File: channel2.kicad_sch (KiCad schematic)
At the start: 33 parts

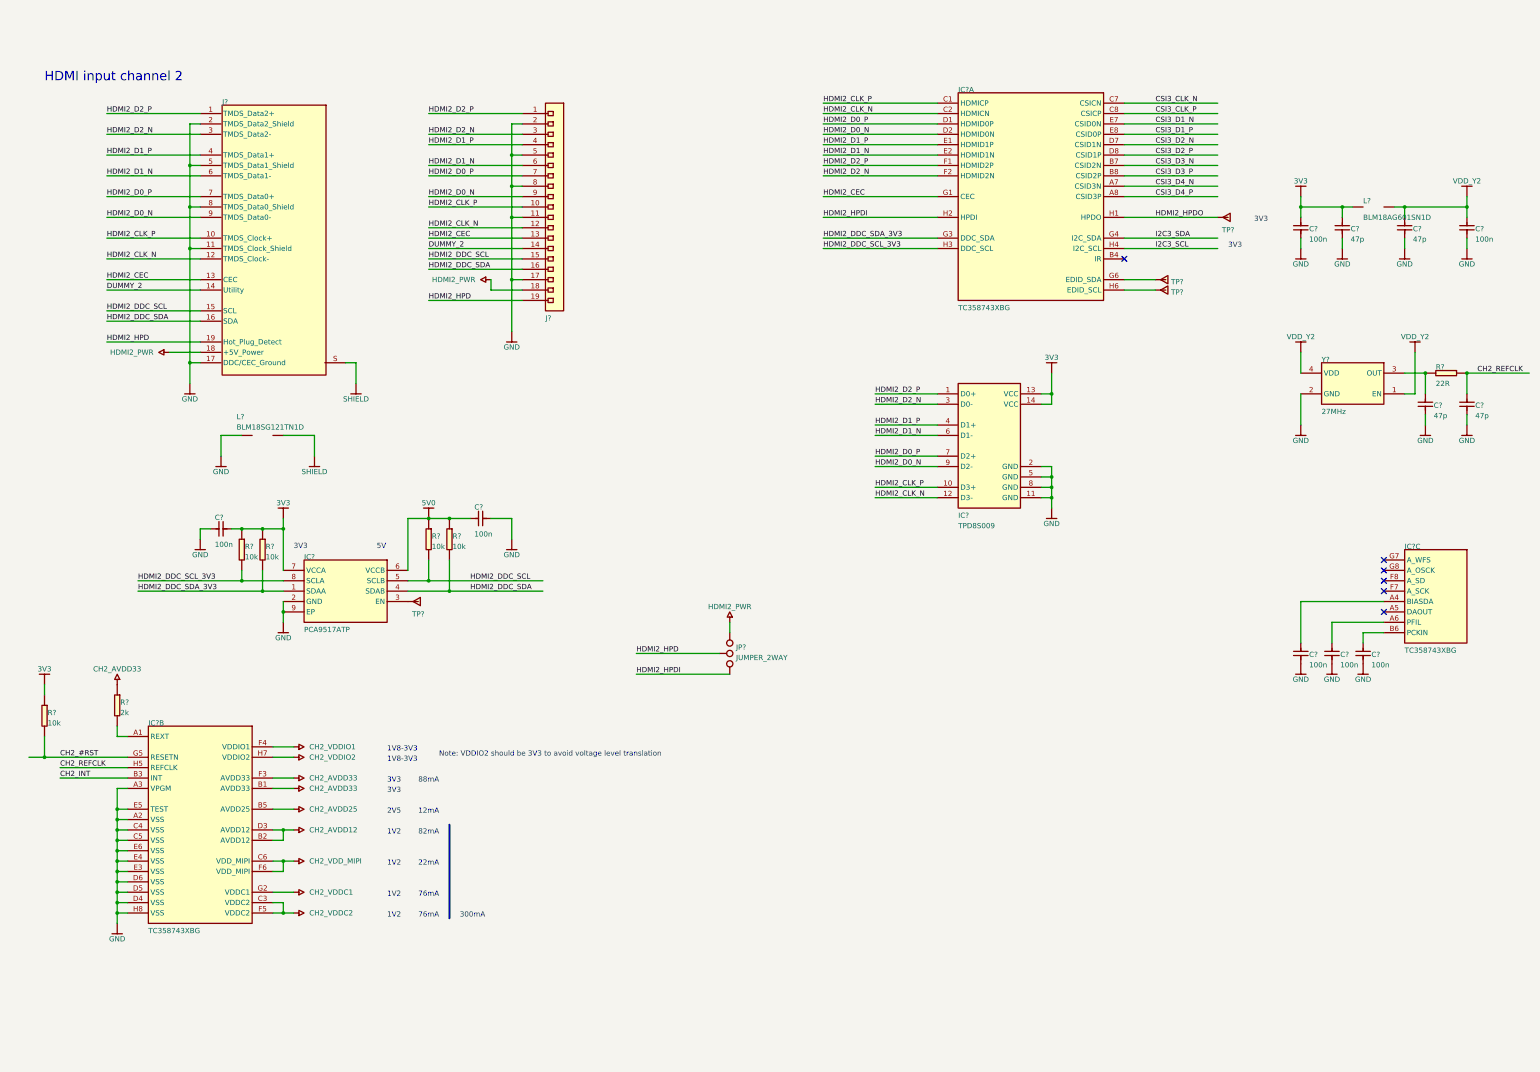
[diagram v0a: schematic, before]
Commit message: Change components to antmicro library ones
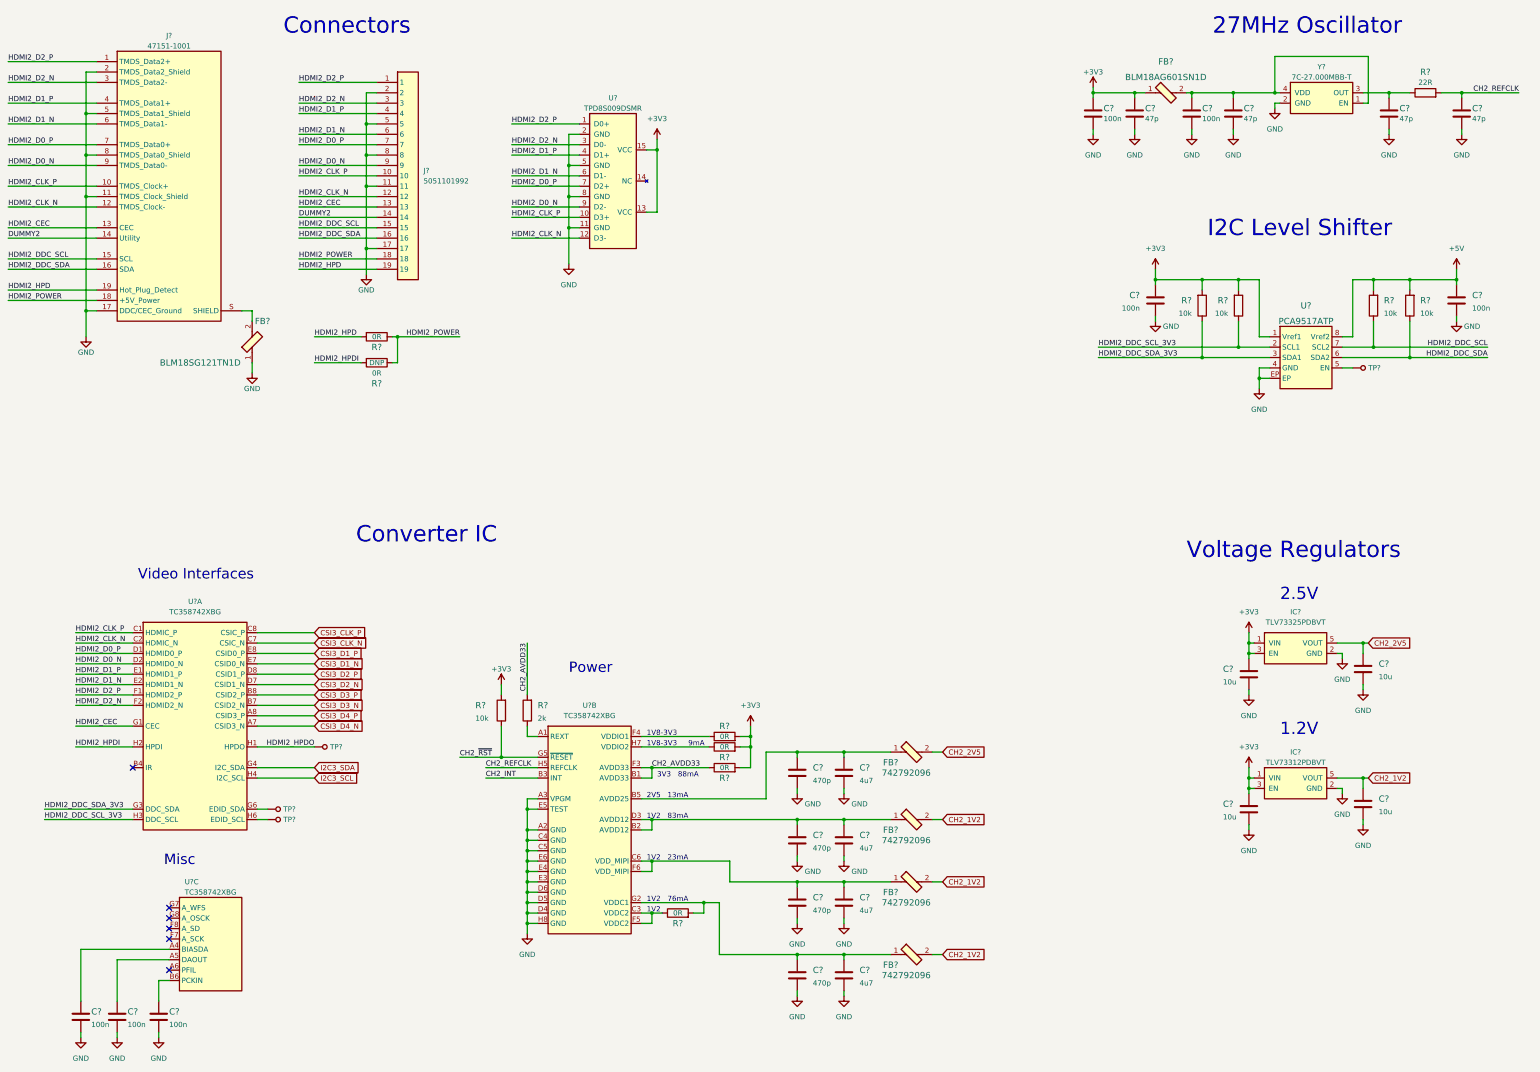
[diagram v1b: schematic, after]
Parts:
- removed C? (x9): ${ALTIUM_VALUE}, HDMI-MIPI-Bridge.Pcblib:0402, symbol altium_import-altium-import:1_C
- removed C? (x2): ${ALTIUM_VALUE}, HDMI-MIPI-Bridge.Pcblib:0402, symbol altium_import-altium-import:2_C
- removed IC?: ${ALTIUM_VALUE}, HDMI-MIPI-Bridge.Pcblib:SON-15, symbol altium_import-altium-import:0_TPD8S009
- removed IC? (x3): ${ALTIUM_VALUE}, HDMI-MIPI-Bridge.Pcblib:TC358743XBG, symbol altium_import-altium-import:0_TC358743XBG
- removed IC?: ${ALTIUM_VALUE}, HDMI-MIPI-Bridge.Pcblib:PCA9517ATP, symbol altium_import-altium-import:0_PCA9517ATP
- removed J?: ${ALTIUM_VALUE}, HDMI-MIPI-Bridge.Pcblib:Molex_HDMI_471511001, symbol altium_import-altium-import:0_CON-Molex-471511001
- removed J?: ${ALTIUM_VALUE}, HDMI-MIPI-Bridge.Pcblib:CON-Molex-505110-1992, symbol altium_import-altium-import:0_1X19
- removed JP?: JUMPER_2WAY, HDMI-MIPI-Bridge.Pcblib:JUMPER_2WAY, symbol altium_import-altium-import:3_JUMPER_2WAY
- removed L? (x2): ${ALTIUM_VALUE}, HDMI-MIPI-Bridge.Pcblib:0603, symbol altium_import-altium-import:0_Inductor SMT
- removed R? (x5): ${ALTIUM_VALUE}, HDMI-MIPI-Bridge.Pcblib:0402, symbol altium_import-altium-import:1_R
- removed R?: ${ALTIUM_VALUE}, HDMI-MIPI-Bridge.Pcblib:0402, symbol altium_import-altium-import:0_R
- removed R?: ${ALTIUM_VALUE}, HDMI-MIPI-Bridge.Pcblib:0603, symbol altium_import-altium-import:1_R
- removed TP? (x4): Testpad, HDMI-MIPI-Bridge.Pcblib:TP-R-1, symbol altium_import-altium-import:3_Testpad
- removed Y?: ${ALTIUM_VALUE}, HDMI-MIPI-Bridge.Pcblib:TXC_7C, symbol altium_import-altium-import:0_TXC_7C
- added C? (x4): C_4u7_0603, antmicro-footprints:0603-cap, symbol antmicroCapacitors0603:C_4u7_0603
- added C? (x7): C_100n_0402, antmicro-footprints:0402-cap, symbol antmicroCapacitors0402:C_100n_0402
- added C? (x4): C_47p_0402, antmicro-footprints:0402-cap, symbol antmicroCapacitors0402:C_47p_0402
- added C? (x4): C_10u_0603, antmicro-footprints:0603-cap, symbol antmicroCapacitors0603:C_10u_0603
- added C? (x4): C_470p_0402, antmicro-footprints:0402-cap, symbol antmicroCapacitors0402:C_470p_0402
- added FB?: BLM18AG601SN1D, antmicro-footprints:0603, symbol antmicroFerriteBeadsandChips:BLM18AG601SN1D
- added FB? (x4): 742792096, antmicro-footprints:0805-res, symbol antmicroFerriteBeadsandChips:742792096
- added FB?: BLM18SG121TN1D, antmicro-footprints:0603-res, symbol antmicroFerriteBeadsandChips:BLM18SG121TN1D
- added IC?: TLV73312PDBVT, antmicro-footprints:SOT-23-5, symbol antmicroPMICVoltageRegulatorsLinear:TLV73312PDBVT
- added IC?: TLV73325PDBVT, antmicro-footprints:SOT-23-5, symbol antmicroPMICVoltageRegulatorsLinear:TLV73325PDBVT
- added J?: 5051101992, antmicro-footprints:5051101992, symbol antmicroFCCConnectors:5051101992
- added J?: 47151-1001, antmicro-footprints:47151-1001, symbol antmicroUSBDVIHDMIConnectors:47151-1001
- added R? (x6): R_0R_0603, antmicro-footprints:0603-res, symbol antmicroResistors0603:R_0R_0603
- added R? (x5): R_10k_0402, antmicro-footprints:0402-res, symbol antmicroResistors0402:R_10k_0402
- added R?: R_22R_0402, antmicro-footprints:0402-res, symbol antmicroResistors0402:R_22R_0402
- added R?: R_2k_0402, antmicro-footprints:0402-res, symbol antmicroResistors0402:R_2k_0402
- added TP? (x4): TP_SMD_0_75MM, antmicro-footprints:Testpoint_smd_0_75mm, symbol antmicroTestPoints:TP_SMD_0_75MM
- added U? (x3): TC358742XBG, antmicro-footprints:BGA-64_8x8_6.0x6.0mm, symbol antmicroInterfaceControllers:TC358742XBG
- added U?: PCA9517ATP, antmicro-footprints:SOT1069-2, symbol antmicroLogicTranslatorsLevelShifters:PCA9517ATP
- added U?: TPD8S009DSMR, antmicro-footprints:R-PDSO-N15, symbol antmicroTVSDiodes:TPD8S009DSMR
- added Y?: 7C-27.000MBB-T, antmicro-footprints:7C-24.000MBB-T, symbol antmicroOscillators:7C-27.000MBB-T
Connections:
- net CH2_AVDD33: now also R?.1, R?.2, U?.B1 (AVDD33), U?.F3 (AVDD33)
- net CH2_INT: now also U?.B3 (INT)
- net CH2_REFCLK: now also C?.1, R?.2, U?.H5 (REFCLK)
- net CSI3_CLK_N: now also U?.C7 (CSIC_N)
- net CSI3_CLK_P: now also U?.C8 (CSIC_P)
- net CSI3_D1_N: now also U?.E7 (CSID0_N)
- net CSI3_D1_P: now also U?.E8 (CSID0_P)
- net CSI3_D2_N: now also U?.D7 (CSID1_N)
- net CSI3_D2_P: now also U?.D8 (CSID1_P)
- net CSI3_D3_N: now also U?.B7 (CSID2_N)
- net CSI3_D3_P: now also U?.B8 (CSID2_P)
- net CSI3_D4_N: now also U?.A7 (CSID3_N)
- net CSI3_D4_P: now also U?.A8 (CSID3_P)
- net GND: now also C?.1, C?.1, C?.1, C?.1, C?.2, C?.2, C?.2, C?.2, C?.2, C?.2, C?.2, C?.2, C?.2, C?.2, C?.2, C?.2, C?.2, C?.2, C?.2, C?.2, C?.2, C?.2, C?.2, FB?.1, IC?.2 (GND), IC?.2 (GND), J?.11, J?.11 (TMDS_Clock_Shield), J?.17, J?.17 (DDC/CEC_Ground), J?.2, J?.2 (TMDS_Data2_Shield), J?.5, J?.5 (TMDS_Data1_Shield), J?.8, J?.8 (TMDS_Data0_Shield), U?.11 (GND), U?.2 (GND), U?.4 (GND), U?.5 (GND), U?.8 (GND), U?.A2 (GND), U?.A3 (VPGM), U?.C4 (GND), U?.C5 (GND), U?.D4 (GND), U?.D5 (GND), U?.D6 (GND), U?.E3 (GND), U?.E4 (GND), U?.E5 (TEST), U?.E6 (GND), U?.EP, U?.H8 (GND), Y?.2 (GND)
- net HDMI2_CEC: now also J?.13, J?.13 (CEC), U?.G1 (CEC)
- net HDMI2_CLK_N: now also J?.12, J?.12 (TMDS_Clock-), U?.12 (D3-), U?.C2 (HDMIC_N)
- net HDMI2_CLK_P: now also J?.10, J?.10 (TMDS_Clock+), U?.10 (D3+), U?.C1 (HDMIC_P)
- net HDMI2_D0_N: now also J?.9, J?.9 (TMDS_Data0-), U?.9 (D2-), U?.D2 (HDMID0_N)
- net HDMI2_D0_P: now also J?.7, J?.7 (TMDS_Data0+), U?.7 (D2+), U?.D1 (HDMID0_P)
- net HDMI2_D1_N: now also J?.6, J?.6 (TMDS_Data1-), U?.6 (D1-), U?.E2 (HDMID1_N)
- net HDMI2_D1_P: now also J?.4, J?.4 (TMDS_Data1+), U?.4 (D1+), U?.E1 (HDMID1_P)
- net HDMI2_D2_N: now also J?.3, J?.3 (TMDS_Data2-), U?.3 (D0-), U?.F2 (HDMID2_N)
- net HDMI2_D2_P: now also J?.1, J?.1 (TMDS_Data2+), U?.1 (D0+), U?.F1 (HDMID2_P)
- net HDMI2_DDC_SCL: now also J?.15, J?.15 (SCL), R?.1, U?.7 (SCL2)
- net HDMI2_DDC_SCL_3V3: now also R?.1, U?.2 (SCL1), U?.H3 (DDC_SCL)
- net HDMI2_DDC_SDA: now also J?.16, J?.16 (SDA), R?.1, U?.6 (SDA2)
- net HDMI2_DDC_SDA_3V3: now also R?.1, U?.3 (SDA1), U?.G3 (DDC_SDA)
- net HDMI2_HPD: now also J?.19, J?.19 (Hot_Plug_Detect), R?.2
- net HDMI2_HPDI: now also R?.2, U?.H2 (HPDI)
- net HDMI2_HPDO: now also TP?.1, U?.H1 (HPDO)
- net I2C3_SCL: now also U?.H4 (I2C_SCL)
- net I2C3_SDA: now also U?.G4 (I2C_SDA)
- new net: C?.1, C?.1, FB?.2, Y?.1 (EN), Y?.4 (VDD)
- new net: C?.1, C?.2, FB?.1, U?.C6 (VDD_MIPI), U?.F6 (VDD_MIPI)
- new net: C?.1, U?.A4 (BIASDA)
- new net: C?.1, C?.2, FB?.1, U?.B5 (AVDD25)
- new net: TP?.1, U?.G6 (EDID_SDA)
- new net: TP?.1, U?.H6 (EDID_SCL)
- new net: C?.1, C?.2, FB?.1, U?.B2 (AVDD12), U?.D3 (AVDD12)
- new net: C?.1, R?.1, Y?.3 (OUT)
- new net: TP?.1, U?.5 (EN)
- new net: R?.1, U?.H7 (VDDIO2)
- new net: C?.1, C?.2, FB?.1, R?.2, U?.G2 (VDDC1)
- new net: FB?.2, J?.S (SHIELD)
- new net: R?.1, U?.C3 (VDDC2), U?.F5 (VDDC2)
- new net: C?.1, U?.A5 (DAOUT)
- new net: C?.1, U?.B6 (PCKIN)
- new net: R?.1, U?.A1 (REXT)
- new net: R?.1, U?.F4 (VDDIO1)
- new net +3V3: C?.1, C?.1, C?.1, C?.1, C?.1, FB?.1, IC?.1 (VIN), IC?.1 (VIN), IC?.3 (EN), IC?.3 (EN), R?.2, R?.2, R?.2, R?.2, R?.2, R?.2, U?.1 (Vref1), U?.13 (VCC), U?.15 (VCC)
- new net +5V: C?.1, R?.2, R?.2, U?.8 (Vref2)
- new net CH2_1V2: C?.1, FB?.2, FB?.2, FB?.2, IC?.5 (VOUT)
- new net CH2_2V5: C?.1, FB?.2, IC?.5 (VOUT)
- new net CH2_~{RST}: R?.1, U?.G5 (~{RESET})
- new net DUMMY2: J?.14, J?.14 (Utility)
- new net HDMI2_POWER: J?.18, J?.18 (+5V_Power), R?.1, R?.1
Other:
- note added: "1.2V"
- note added: "13mA"
- note added: "2.5V"
- note added: "23mA"
- note added: "27MHz Oscillator"
- note added: "83mA"
- note added: "9mA"
- note added: "Connectors"
- note added: "Converter IC"
- note added: "I2C Level Shifter"
- note added: "Misc"
- note added: "Power"
- note added: "Video Interfaces"
- note added: "Voltage Regulators"
- note removed: "12mA"
- note removed: "22mA"
- note removed: "300mA"
- note removed: "5V"
- note removed: "82mA"
- note removed: "HDMI input channel 2"
- note removed: "Note: VDDIO2 should be 3V3 to avoid voltage level translation"

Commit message: Layout of the PCB
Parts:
- removed C? (x4): C_4u7_0603, antmicro-footprints:0603-cap, symbol antmicroCapacitors0603:C_4u7_0603
- removed C? (x4): C_470p_0402, antmicro-footprints:0402-cap, symbol antmicroCapacitors0402:C_470p_0402
- removed FB? (x4): 742792096, antmicro-footprints:0805-res, symbol antmicroFerriteBeadsandChips:742792096
- removed R? (x4): R_0R_0603, antmicro-footprints:0603-res, symbol antmicroResistors0603:R_0R_0603
- added C31, C32, C33, C34: C_100n_0402, antmicro-footprints:0402-cap, symbol antmicroCapacitors0402:C_100n_0402
- added C47, C48, C49, C50: C_470p_0402, antmicro-footprints:0402-cap, symbol antmicroCapacitors0402:C_470p_0402
- added C51, C52, C53, C54: C_4u7_0603, antmicro-footprints:0603-cap, symbol antmicroCapacitors0603:C_4u7_0603
- added FB10, FB11, FB8, FB9: 742792096, antmicro-footprints:0805-res, symbol antmicroFerriteBeadsandChips:742792096
- added R18, R19, R20, R21: R_0R_0603, antmicro-footprints:0603-res, symbol antmicroResistors0603:R_0R_0603
- C36, C44, C46: renamed from C?; DNP (none) -> DNP
- gave numbers to parts that had none: 35
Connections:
- net +3V3: now also R19.2, R20.2, R21.2
- net CH2_1V2: now also FB10.2, FB11.2, FB9.2
- net CH2_2V5: now also FB8.2
- net CH2_AVDD33: now also C34.1, R21.1
- net GND: now also C31.2, C32.2, C33.2, C34.2, C47.1, C48.1, C49.1, C50.1, C51.2, C52.2, C53.2, C54.2
- net at U4.C6 (VDD_MIPI), U4.F6 (VDD_MIPI): now also C49.2, C53.1, FB10.1
- net at U4.B5 (AVDD25): now also C47.2, C51.1, FB8.1
- net at U4.B2 (AVDD12), U4.D3 (AVDD12): now also C48.2, C52.1, FB9.1
- net at U4.H7 (VDDIO2): now also C33.1, R20.1
- net at U4.G2 (VDDC1): now also C50.2, C54.1, FB11.1, R18.2
- net at U4.C3 (VDDC2), U4.F5 (VDDC2): now also C31.1, R18.1
- net at U4.F4 (VDDIO1): now also C32.1, R19.1
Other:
- moved on the sheet: C24, C25, C26, TP5, TP6, TP7, U4A, U4C

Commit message: Revision bump to 1.3.0
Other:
- title: (none) -> Antmicro HDMI MIPI Bridge
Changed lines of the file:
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@@
 (kicad_sch (version 20211123) (generator eeschema)
   (paper "A3")
+  (title_block
+    (title "Antmicro HDMI MIPI Bridge")
+    (date "2023-03-02")
+    (rev "1.3.0")
+  )
   (junction (at 156.21 242.57) (diameter 0) (color 0 0 0 0)
   )

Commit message: Schematic cleanup
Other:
- moved on the sheet: C24, C25, C26, U4C

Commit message: Update local library of components
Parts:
- C24, C25, C26, C31, C32, C33, C34, C35, C37, C38, C45: footprint antmicro-footprints:0402-cap -> antmicro-hdmi-mipi-bridge-hw-footprints:0402-cap; symbol antmicroCapacitors0402:C_100n_0402 -> antmicro-hdmi-mipi-bridge-hw:C_100n_0402
- C36, C39, C44, C46: footprint antmicro-footprints:0402-cap -> antmicro-hdmi-mipi-bridge-hw-footprints:0402-cap; symbol antmicroCapacitors0402:C_47p_0402 -> antmicro-hdmi-mipi-bridge-hw:C_47p_0402
- C40, C41, C42, C43: footprint antmicro-footprints:0603-cap -> antmicro-hdmi-mipi-bridge-hw-footprints:0603-cap; symbol antmicroCapacitors0603:C_10u_0603 -> antmicro-hdmi-mipi-bridge-hw:C_10u_0603
- C47, C48, C49, C50: footprint antmicro-footprints:0402-cap -> antmicro-hdmi-mipi-bridge-hw-footprints:0402-cap; symbol antmicroCapacitors0402:C_470p_0402 -> antmicro-hdmi-mipi-bridge-hw:C_470p_0402
- C51, C52, C53, C54: footprint antmicro-footprints:0603-cap -> antmicro-hdmi-mipi-bridge-hw-footprints:0603-cap; symbol antmicroCapacitors0603:C_4u7_0603 -> antmicro-hdmi-mipi-bridge-hw:C_4u7_0603
- FB10, FB11, FB8, FB9: footprint antmicro-footprints:0805-res -> antmicro-hdmi-mipi-bridge-hw-footprints:0805-res; symbol antmicroFerriteBeadsandChips:742792096 -> antmicro-hdmi-mipi-bridge-hw:742792096
- FB12: footprint antmicro-footprints:0603 -> antmicro-hdmi-mipi-bridge-hw-footprints:0603; symbol antmicroFerriteBeadsandChips:BLM18AG601SN1D -> antmicro-hdmi-mipi-bridge-hw:BLM18AG601SN1D
- FB7: footprint antmicro-footprints:0603-res -> antmicro-hdmi-mipi-bridge-hw-footprints:0603-res; symbol antmicroFerriteBeadsandChips:BLM18SG121TN1D -> antmicro-hdmi-mipi-bridge-hw:BLM18SG121TN1D
- IC3: footprint antmicro-footprints:SOT-23-5 -> antmicro-hdmi-mipi-bridge-hw-footprints:SOT-23-5; symbol antmicroPMICVoltageRegulatorsLinear:TLV73325PDBVT -> antmicro-hdmi-mipi-bridge-hw:TLV73325PDBVT
- IC4: footprint antmicro-footprints:SOT-23-5 -> antmicro-hdmi-mipi-bridge-hw-footprints:SOT-23-5; symbol antmicroPMICVoltageRegulatorsLinear:TLV73312PDBVT -> antmicro-hdmi-mipi-bridge-hw:TLV73312PDBVT
- J4: footprint antmicro-footprints:47151-1001 -> antmicro-hdmi-mipi-bridge-hw-footprints:47151-1001; symbol antmicroUSBDVIHDMIConnectors:47151-1001 -> antmicro-hdmi-mipi-bridge-hw:47151-1001
- J5: footprint antmicro-footprints:5051101992 -> antmicro-hdmi-mipi-bridge-hw-footprints:5051101992; symbol antmicroFCCConnectors:5051101992 -> antmicro-hdmi-mipi-bridge-hw:5051101992
- R14, R15, R18, R19, R20, R21: footprint antmicro-footprints:0603-res -> antmicro-hdmi-mipi-bridge-hw-footprints:0603-res; symbol antmicroResistors0603:R_0R_0603 -> antmicro-hdmi-mipi-bridge-hw:R_0R_0603
- R16, R22, R23, R24, R25: footprint antmicro-footprints:0402-res -> antmicro-hdmi-mipi-bridge-hw-footprints:0402-res; symbol antmicroResistors0402:R_10k_0402 -> antmicro-hdmi-mipi-bridge-hw:R_10k_0402
- R17: footprint antmicro-footprints:0402-res -> antmicro-hdmi-mipi-bridge-hw-footprints:0402-res; symbol antmicroResistors0402:R_2k_0402 -> antmicro-hdmi-mipi-bridge-hw:R_2k_0402
- R26: footprint antmicro-footprints:0402-res -> antmicro-hdmi-mipi-bridge-hw-footprints:0402-res; symbol antmicroResistors0402:R_22R_0402 -> antmicro-hdmi-mipi-bridge-hw:R_22R_0402
- TP5, TP6, TP7, TP8: footprint antmicro-footprints:Testpoint_smd_0_75mm -> antmicro-hdmi-mipi-bridge-hw-footprints:Testpoint_smd_0_75mm; symbol antmicroTestPoints:TP_SMD_0_75MM -> antmicro-hdmi-mipi-bridge-hw:TP_SMD_0_75MM
- U4: footprint antmicro-footprints:BGA-64_8x8_6.0x6.0mm -> antmicro-hdmi-mipi-bridge-hw-footprints:BGA-64_8x8_6.0x6.0mm; symbol antmicroInterfaceControllers:TC358742XBG -> antmicro-hdmi-mipi-bridge-hw:TC358742XBG
- U5: footprint antmicro-footprints:R-PDSO-N15 -> antmicro-hdmi-mipi-bridge-hw-footprints:R-PDSO-N15; symbol antmicroTVSDiodes:TPD8S009DSMR -> antmicro-hdmi-mipi-bridge-hw:TPD8S009DSMR
- U6: footprint antmicro-footprints:SOT1069-2 -> antmicro-hdmi-mipi-bridge-hw-footprints:SOT1069-2; symbol antmicroLogicTranslatorsLevelShifters:PCA9517ATP -> antmicro-hdmi-mipi-bridge-hw:PCA9517ATP
- Y2: footprint antmicro-footprints:7C-24.000MBB-T -> antmicro-hdmi-mipi-bridge-hw-footprints:7C-24.000MBB-T; symbol antmicroOscillators:7C-27.000MBB-T -> antmicro-hdmi-mipi-bridge-hw:7C-27.000MBB-T
